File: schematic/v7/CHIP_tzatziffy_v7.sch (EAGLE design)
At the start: 56 parts, among them J1 2X20-CHIP0.7_DRILL, Q2 2N7002ET1G, U1 LMR62421, U3 DS2431P, X1 FH12-40S-0.5SH

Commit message: added power supply
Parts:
- removed CHRIN: (no value), wirepad:1,6/0,8
- removed CHRIN_P: CHRIN, wirepad:SMD5
- added PG, PV: (no value), wirepad:1,6/0,8
- added U$10: MP1584EN, JKW_CHIP:MP1584EN
- SJ3, SJ4: value (none) -> SMD_SJ_3WAY_CLOSED; device SparkFun-Retired:SOLDERJUMPER_2WAYT -> JKW_CHIP:SMD_SJ_3WAY_CLOSED
- renumbered VB to BV
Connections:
- net N$26 renamed VCC3V3_2
- new net AMP_PWR: C11.2, C12.2, C15.1, PAM1.MUTE, PAM1.PVDD, PAM1.PVDD1, PAM1.VDD, SJ3.2
- new net DC_IN: C2.1, C4.1, L1.2, L2.2, SJ1.2, SJ4.2, U1.VIN
- new net PWR_IN: PV.P, U$10.VIN
- net GND: now also PG.P, U$10.GNDIN, U$10.GNDOUT
- net VCC3V3: now also SJ3.1; no longer C11.2, C12.2, C15.1, PAM1.MUTE, PAM1.PVDD, PAM1.PVDD1, PAM1.VDD, SJ3.2, SJ3.3
- net VCC5V: now also SJ3.3; no longer SJ3.1
- net VOUT: now also U$10.VOUT; no longer C2.1, C4.1, CHRIN.P, CHRIN_P.P, L1.2, L2.2, SJ1.2, SJ4.2, U1.VIN
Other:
- note removed: "cut here ->"
- moved on the sheet: BTN, GND

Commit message: optimized routing and schematic
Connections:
- net N$1 renamed SDIO_DAT0
- net N$25 renamed SDIO_CMD
- net N$27 renamed SDIO_DAT1
- net N$28 renamed SDIO_DAT3
- net N$31 renamed SDIO_DAT2
- net N$37 renamed AUDIO_R
- net N$40 renamed AUDIO_L
- net N$44 renamed SDIO_CLK
- net N$45 renamed SDIO_CARD
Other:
- note added: "Audio"
- note added: "DC/DC converter"
- note added: "Display Pinout according to: CT43C4827WQ24 TST430MINI-05DP"
- note added: "Power Connection"
- note removed: "Backup Battery Connection"
- note removed: "LCD FPC Connector"
- note removed: "Pinout according to: CT43C4827WQ24 TST430MINI-05DP"
- note removed: "VDD"
- moved on the sheet: BG, BTN, BV, GND, PG, PV, Q2, R13, SJ1, SJ4

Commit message: improved routing
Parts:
- U$10: value MP1584EN -> MP1584EN_FRAMELESS; device JKW_CHIP:MP1584EN -> JKW_CHIP:MP1584EN_FRAMELESS
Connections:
- net N$32 renamed L+OUT
- net N$33 renamed L-OUT
- net N$34 renamed R+OUT
- net N$35 renamed R-OUT
- net N$36 renamed INL
- net N$39 renamed INR
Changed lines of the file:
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@@
 <?xml version="1.0" encoding="utf-8"?>
 <!DOCTYPE eagle SYSTEM "eagle.dtd">
-<eagle version="7.6.0">
+<eagle version="7.7.0">
 <drawing>
 <settings>
@@
 <part name="U$9" library="Keyboard v0.2" deviceset="GND" device=""/>
 <part name="SJ4" library="JKW_CHIP" deviceset="SMD_SJ_3WAY_CLOSED" device=""/>
-<part name="U$10" library="JKW_CHIP" deviceset="MP1584EN" device=""/>
+<part name="U$10" library="JKW_CHIP" deviceset="MP1584EN_FRAMELESS" device=""/>
 <part name="U$11" library="Keyboard v0.2" deviceset="GND" device=""/>
 <part name="U$22" library="Keyboard v0.2" deviceset="GND" device=""/>
@@
 </segment>
 </net>
-<net name="N$32" class="0">
+<net name="L+OUT" class="0">
 <segment>
 <wire x1="281.94" y1="266.7" x2="281.94" y2="261.62" width="0.1524" layer="91"/>
@@
 </segment>
 </net>
-<net name="N$33" class="0">
+<net name="L-OUT" class="0">
 <segment>
 <wire x1="292.1" y1="256.54" x2="290.83" y2="256.54" width="0.1524" layer="91"/>
@@
 </segment>
 </net>
-<net name="N$34" class="0">
+<net name="R+OUT" class="0">
 <segment>
 <pinref part="PAM1" gate="G$1" pin="+OUT_R"/>
@@
 </segment>
 </net>
-<net name="N$35" class="0">
+<net name="R-OUT" class="0">
 <segment>
 <pinref part="PAM1" gate="G$1" pin="-OUT_R"/>
@@
 </segment>
 </net>
-<net name="N$36" class="0">
+<net name="INL" class="0">
 <segment>
 <wire x1="292.1" y1="246.38" x2="290.83" y2="246.38" width="0.1524" layer="91"/>
@@
 </segment>
 </net>
-<net name="N$39" class="0">
+<net name="INR" class="0">
 <segment>
 <pinref part="PAM1" gate="G$1" pin="INR"/>

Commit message: improved routing
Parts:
- BTN, GND: device wirepad:SMD5 -> wirepad:SMD2
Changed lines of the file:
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@@
 <part name="D2" library="Keyboard v0_5" deviceset="DIODE_SCHTKY_B240" device="" value="B240A"/>
 <part name="R6" library="rcl" deviceset="R-EU_" device="R0805" value="12k"/>
-<part name="GND" library="wirepad" deviceset="SMD5" device="" value="GND"/>
-<part name="BTN" library="wirepad" deviceset="SMD5" device="" value="BTN"/>
+<part name="GND" library="wirepad" deviceset="SMD2" device="" value="GND"/>
+<part name="BTN" library="wirepad" deviceset="SMD2" device="" value="BTN"/>
 <part name="U$6" library="Keyboard v0.2" deviceset="GND" device=""/>
 <part name="SJ3" library="JKW_CHIP" deviceset="SMD_SJ_3WAY_CLOSED" device=""/>

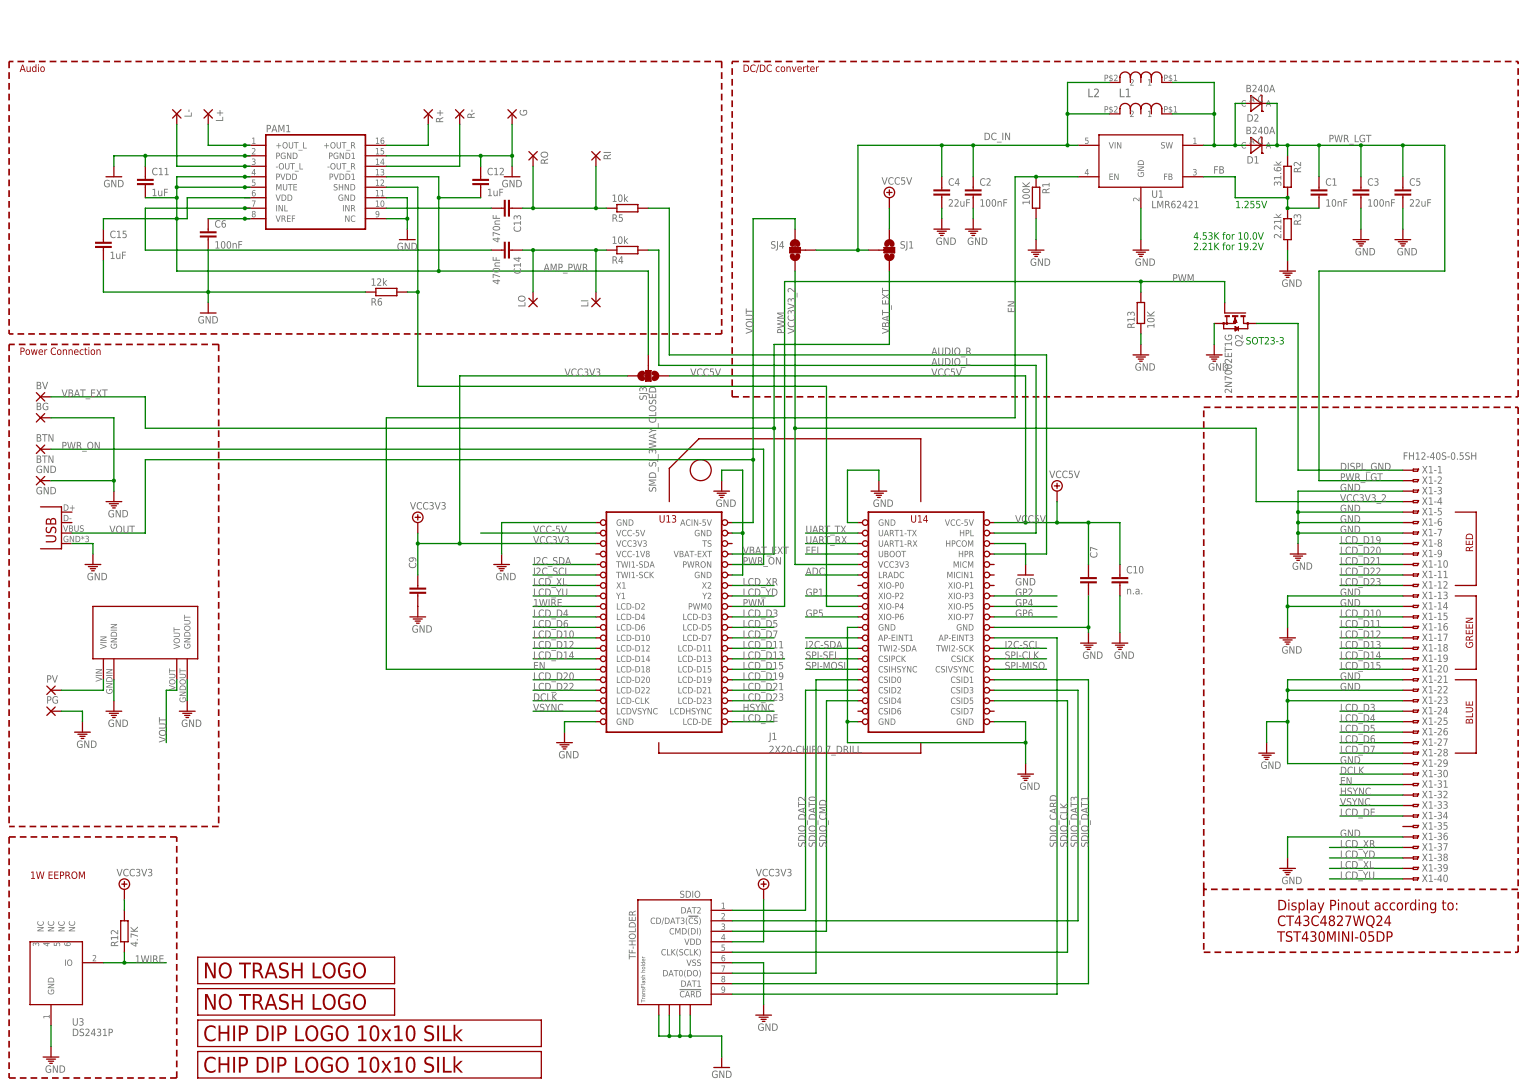
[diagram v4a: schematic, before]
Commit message: added alternate dc/dc switch
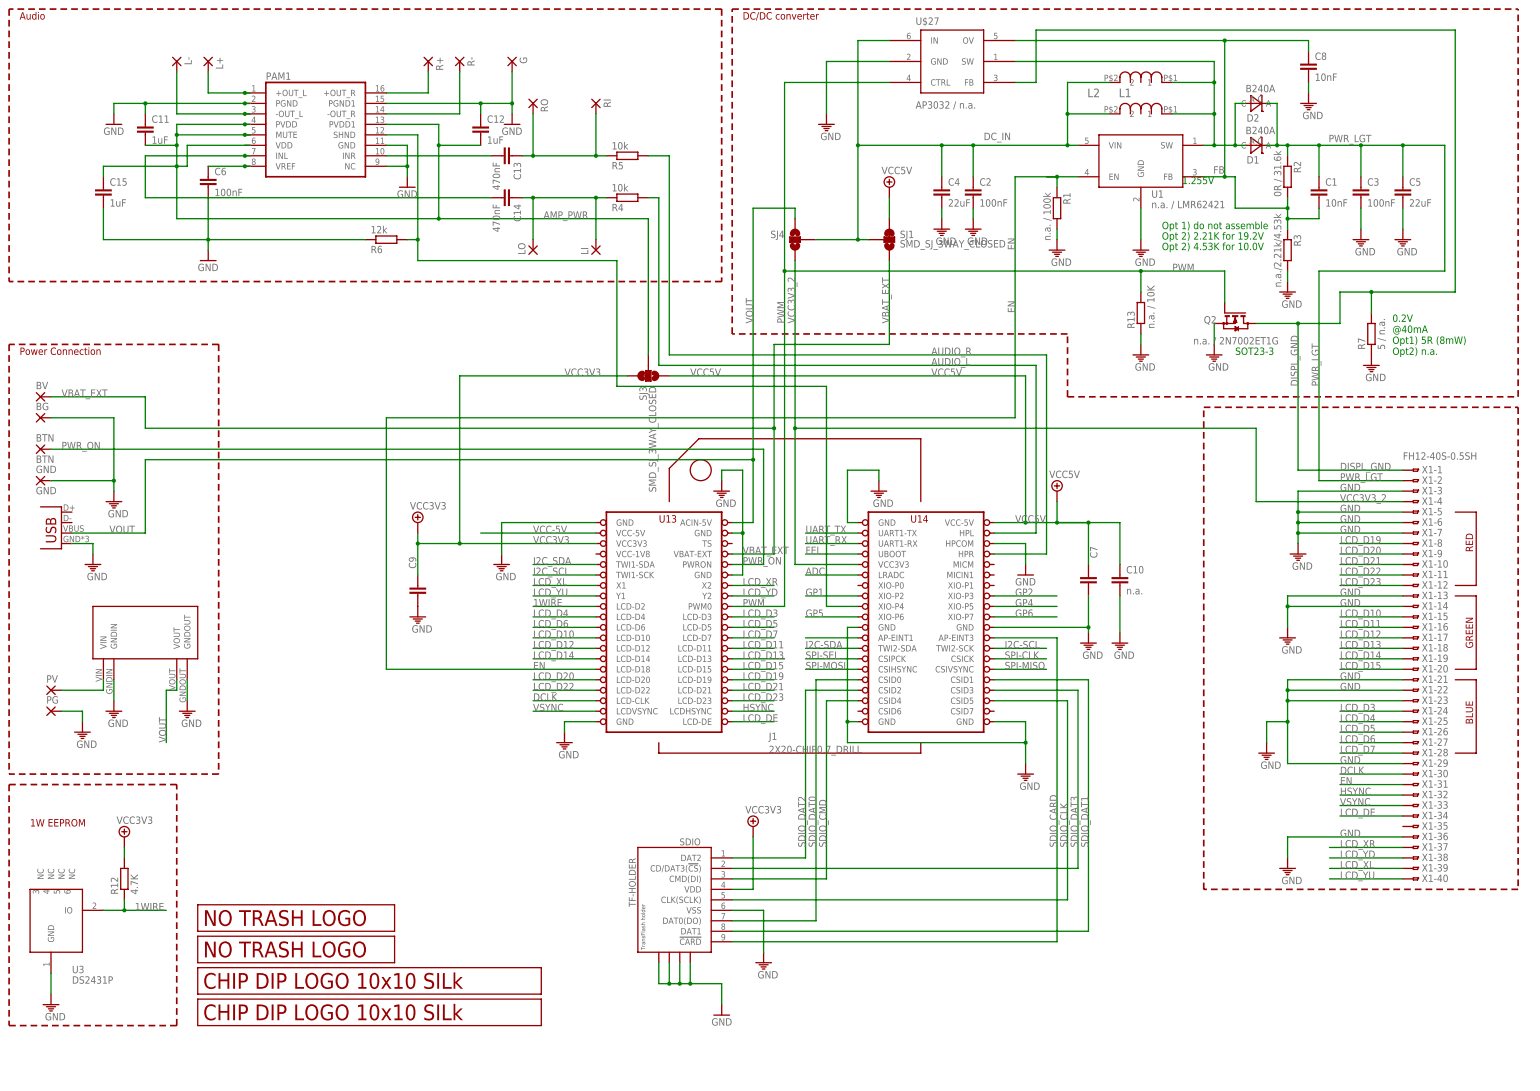
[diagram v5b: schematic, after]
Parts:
- added C8: 10nF, rcl:C-EUC0805
- added R7: 5 / n.a., rcl:R-EU_M0805
- added U$27: AP3032 / n.a., JKW_CHIP:AP3032
- Q2: value 2N7002ET1G -> n.a. / 2N7002ET1G
- R1: value 100K -> n.a. / 100k
- R13: value 10K -> n.a. / 10K
- R2: value 31.6k -> 0R / 31.6k
- R3: value 2.21k -> n.a./2.21k/4.53k
- SJ1: value (none) -> SMD_SJ_3WAY_CLOSED; device SparkFun-Retired:SOLDERJUMPER_2WAYT -> JKW_CHIP:SMD_SJ_3WAY_CLOSED
- SJ4: value SMD_SJ_3WAY_CLOSED -> (none); device JKW_CHIP:SMD_SJ_3WAY_CLOSED -> JKW_CHIP:SMD_SJ_3WAY_OPENT
- U1: value LMR62421 -> n.a. / LMR62421
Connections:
- net DC_IN: now also U$27.IN
- net DISPL_GND: now also R7.2, U$27.FB
- net FB: now also C8.1, U$27.OV
- net GND: now also C8.2, R7.1, U$27.GND
- net PWM: now also U$27.CTRL
- net VREG_OUTPUT: now also U$27.SW
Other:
- note added: "0.2V @40mA Opt1) 5R (8mW) Opt2) n.a."
- note added: "Opt 1) do not assemble"
- note added: "Opt 2) 2.21K for 19.2V"
- note added: "Opt 2) 4.53K for 10.0V"
- note removed: "2.21K for 19.2V"
- note removed: "4.53K for 10.0V"
- note removed: "Display Pinout according to: CT43C4827WQ24 TST430MINI-05DP"
- moved on the sheet: C11, C12, C13, C14, C15, C6, G, L+, L-, LI, LO, PAM1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
